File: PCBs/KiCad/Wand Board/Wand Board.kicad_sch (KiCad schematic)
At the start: 24 parts, among them J1 BRL LEDS, J10 ENC BTN, J11 ENCODER, J12 POW_IN, J13 BRL SENSE, J14 BAR, J15 DISP, J16 USB DATA, J2 BODY LEDS, J3 TIP LED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

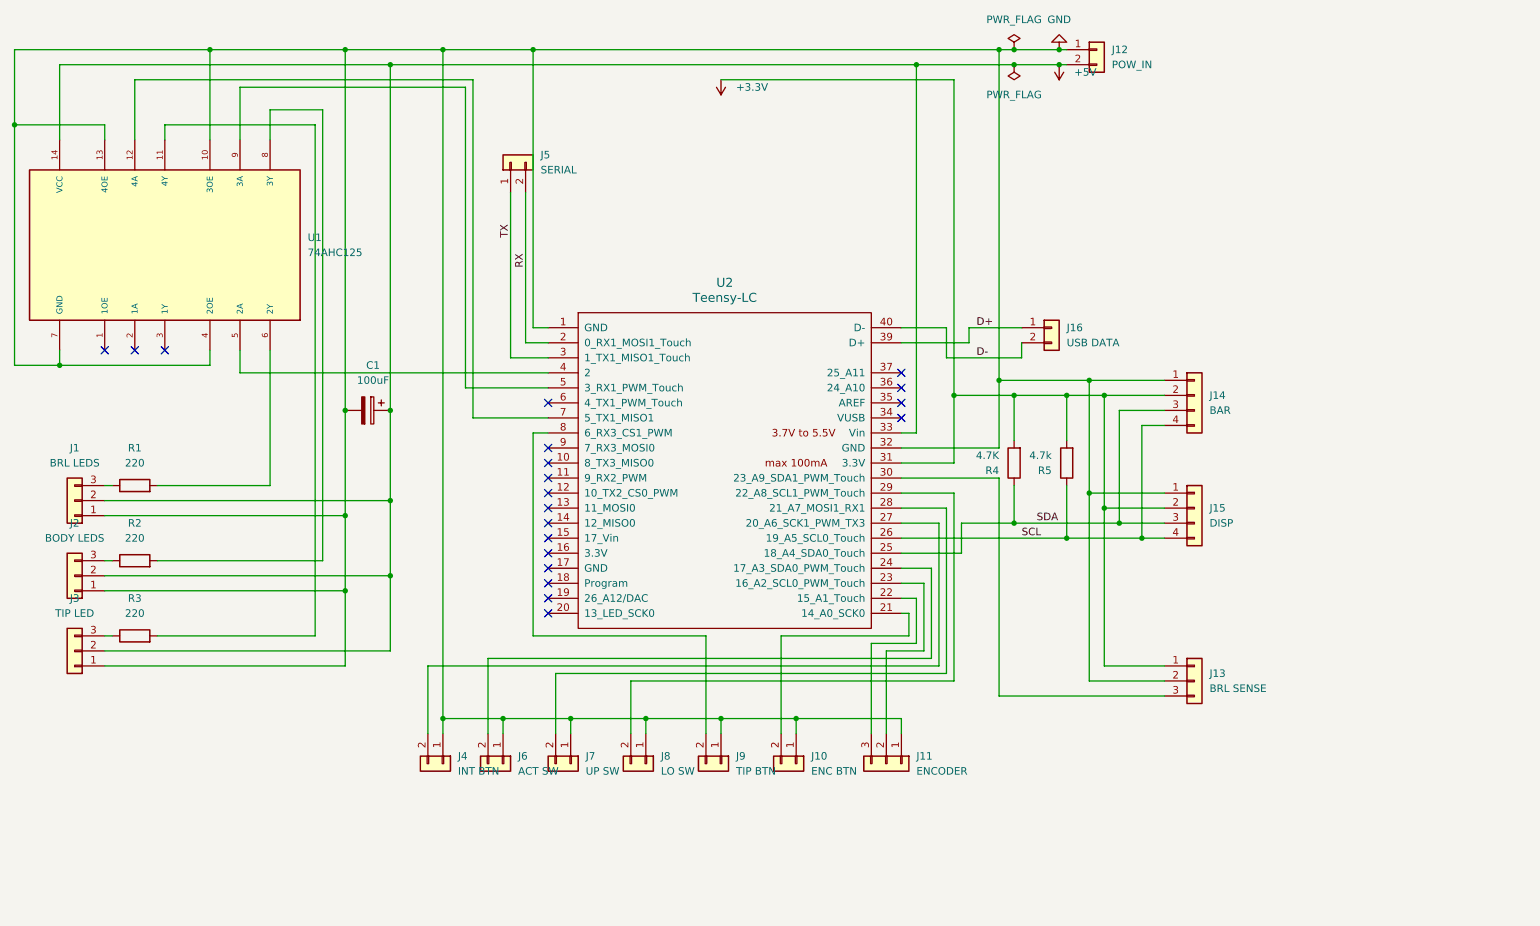
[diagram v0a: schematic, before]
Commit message: Updated Wand Board PCB: Migrate to Teensy 4.0, Change Encoder Pin Order
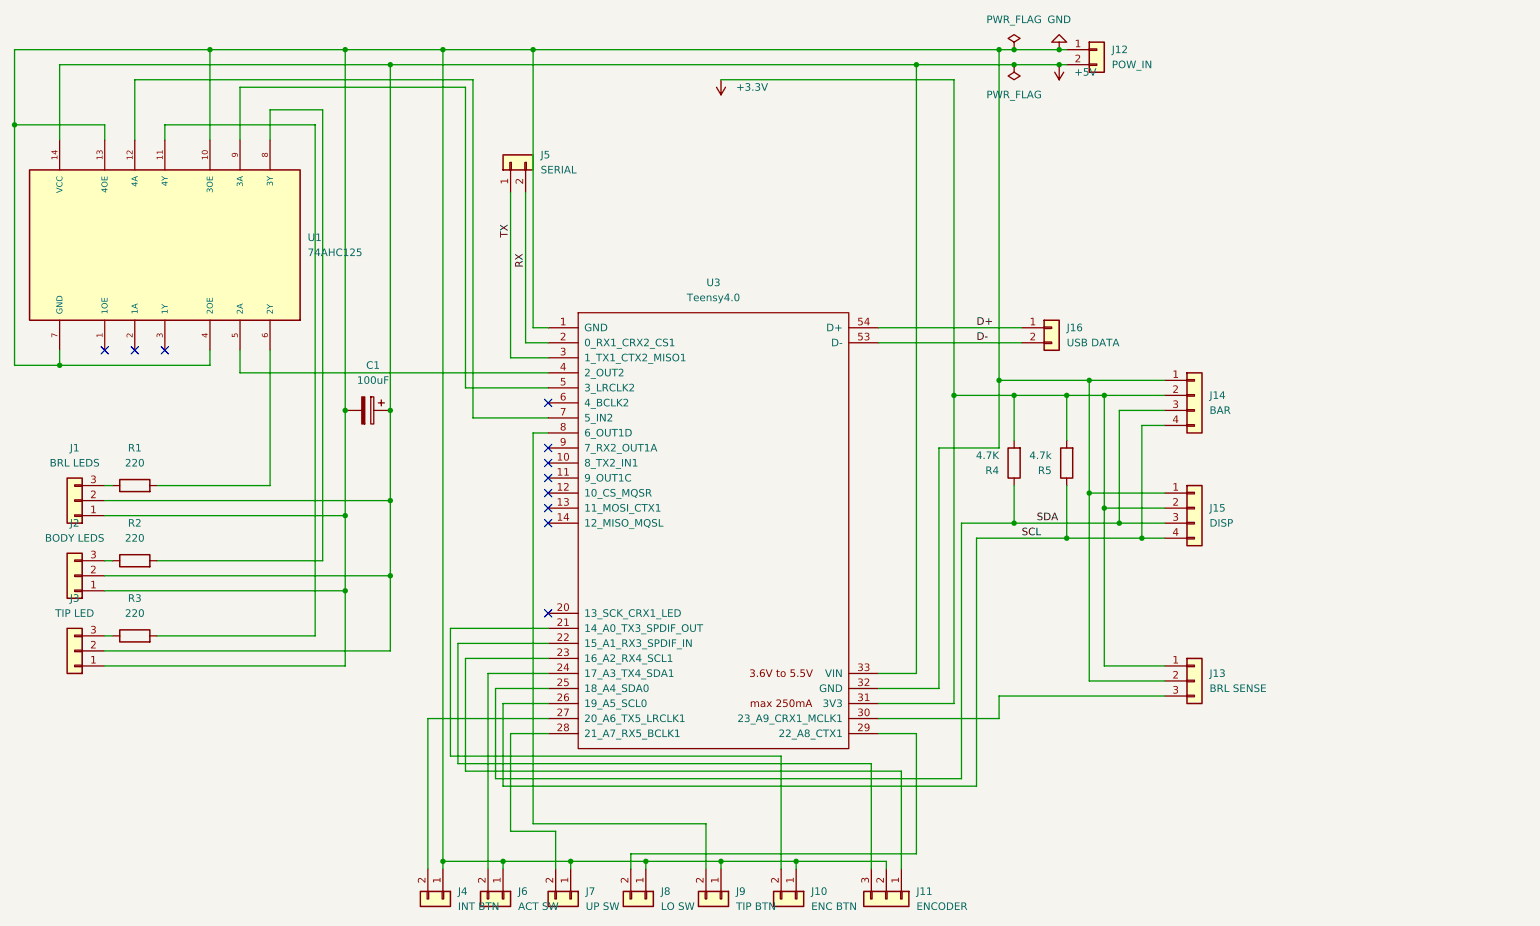
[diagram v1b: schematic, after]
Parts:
- removed U2: Teensy-LC, Teensy:Teensy_LC, symbol teensy:Teensy-LC
- added U3: Teensy4.0, Teensy:Teensy40-DHolesOnly, symbol teensy:Teensy4.0
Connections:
- net +3.3V: now also U3.31 (3V3)
- net +5V: now also U3.33 (VIN)
- net D+: now also U3.54 (D+)
- net D-: now also U3.53 (D-)
- net GND: now also J11.2 (Pin_2), U3.1 (GND), U3.32 (GND); no longer J11.1 (Pin_1)
- net RX: now also U3.2 (0_RX1_CRX2_CS1)
- net SCL: now also U3.26 (19_A5_SCL0)
- net SDA: now also U3.25 (18_A4_SDA0)
- net TX: now also U3.3 (1_TX1_CTX2_MISO1)
- net at J10.2 (Pin_2): now also U3.21 (14_A0_TX3_SPDIF_OUT)
- net at J11.3 (Pin_3): now also U3.22 (15_A1_RX3_SPDIF_IN)
- net at J6.2 (Pin_2): now also U3.24 (17_A3_TX4_SDA1)
- net at J4.2 (Pin_2): now also U3.27 (20_A6_TX5_LRCLK1)
- net at J7.2 (Pin_2): now also U3.28 (21_A7_RX5_BCLK1)
- net at J8.2 (Pin_2): now also U3.29 (22_A8_CTX1)
- net at J13.3 (Pin_3): now also U3.30 (23_A9_CRX1_MCLK1)
- net at U1.5 (2A): now also U3.4 (2_OUT2)
- net at U1.9 (3A): now also U3.5 (3_LRCLK2)
- net at U1.12 (4A): now also U3.7 (5_IN2)
- net at J9.2 (Pin_2): now also U3.8 (6_OUT1D)
- new net: J11.1 (Pin_1), U3.23 (16_A2_RX4_SCL1)
- no-connect marks 20 -> 11
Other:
- moved on the sheet: J10, J11, J4, J6, J7, J8, J9

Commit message: Added motor output for wand rumble
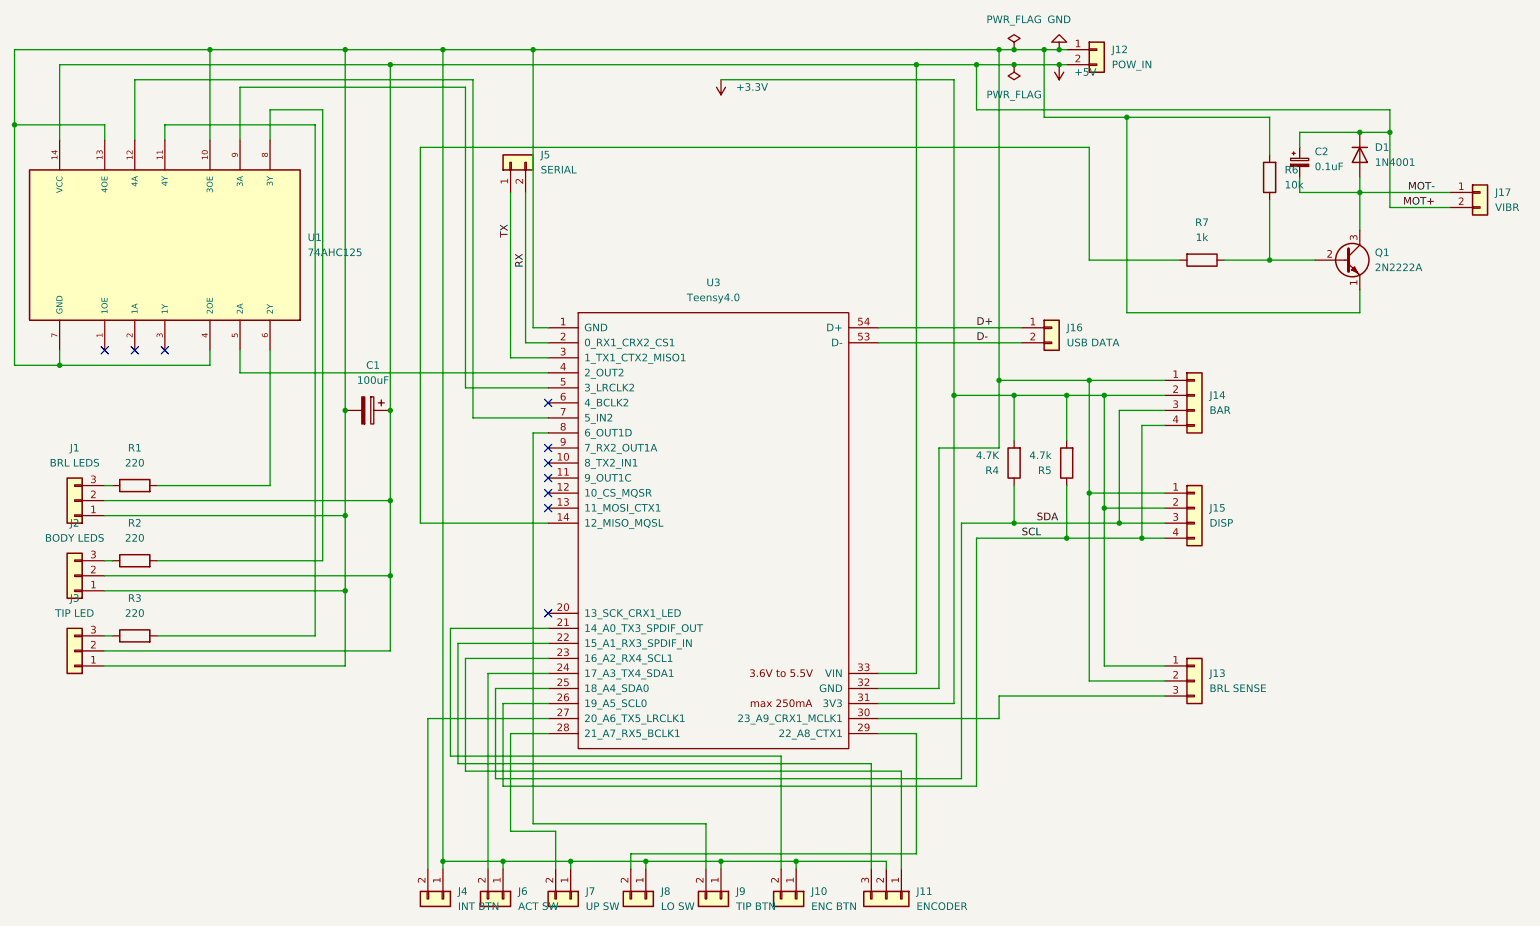
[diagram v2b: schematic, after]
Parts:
- added C2: 0.1uF, Capacitor_THT:CP_Radial_D4.0mm_P2.00mm, symbol Device:C_Polarized_Small
- added D1: 1N4001, Diode_THT:D_DO-41_SOD81_P10.16mm_Horizontal, symbol Diode:1N4001
- added J17: VIBR, Connector_JST:JST_XH_B2B-XH-A_1x02_P2.50mm_Vertical, symbol Connector_Generic:Conn_01x02
- added Q1: 2N2222A, Package_TO_SOT_THT:TO-92_Inline, symbol Transistor_BJT:PN2222A
- added R6: 10k, Resistor_THT:R_Axial_DIN0207_L6.3mm_D2.5mm_P7.62mm_Horizontal, symbol Device:R
- added R7: 1k, Resistor_THT:R_Axial_DIN0207_L6.3mm_D2.5mm_P7.62mm_Horizontal, symbol Device:R
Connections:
- net +5V: now also C2.1, D1.1 (K), J17.2 (Pin_2)
- net GND: now also Q1.1 (E), R6.2
- net at U3.14 (12_MISO_MQSL): now also R7.2
- new net: Q1.2 (B), R6.1, R7.1
- new net MOT-: C2.2, D1.2 (A), J17.1 (Pin_1), Q1.3 (C)
- no-connect marks 11 -> 10

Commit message: Added additional i2c output to wand board for optional driver
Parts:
- added J18: i2c, Connector_JST:JST_XH_B4B-XH-A_1x04_P2.50mm_Vertical, symbol Connector_Generic:Conn_01x04
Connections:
- net +3.3V: now also J18.2 (Pin_2)
- net GND: now also J18.1 (Pin_1)
- net SCL: now also J18.4 (Pin_4)
- net SDA: now also J18.3 (Pin_3)
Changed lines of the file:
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@@
   (junction (at 250.19 31.75) (diameter 0) (color 0 0 0 0)
   )
+  (junction (at 201.93 109.22) (diameter 0) (color 0 0 0 0)
+  )
   (junction (at 199.39 92.71) (diameter 0) (color 0 0 0 0)
   )
   (junction (at 186.69 20.32) (diameter 0) (color 0 0 0 0)
+  )
+  (junction (at 199.39 106.68) (diameter 0) (color 0 0 0 0)
   )
   (junction (at 100.33 154.94) (diameter 0) (color 0 0 0 0)
@@
     (stroke (width 0) (type default))
   )
-  (wire (pts (xy 201.93 95.25) (xy 201.93 121.92))
+  (wire (pts (xy 199.39 106.68) (xy 212.09 106.68))
+    (stroke (width 0) (type default))
+  )
+  (wire (pts (xy 201.93 95.25) (xy 201.93 109.22))
     (stroke (width 0) (type default))
   )
@@
     (stroke (width 0) (type default))
   )
+  (wire (pts (xy 208.28 114.3) (xy 208.28 100.33))
+    (stroke (width 0) (type default))
+  )
   (wire (pts (xy 101.6 41.91) (xy 101.6 69.85))
     (stroke (width 0) (type default))
@@
     (stroke (width 0) (type default))
   )
+  (wire (pts (xy 212.09 114.3) (xy 208.28 114.3))
+    (stroke (width 0) (type default))
+  )
   (wire (pts (xy 163.83 133.35) (xy 170.18 133.35))
     (stroke (width 0) (type default))
@@
     (stroke (width 0) (type default))
   )
-  (wire (pts (xy 199.39 92.71) (xy 199.39 124.46))
+  (wire (pts (xy 199.39 92.71) (xy 199.39 106.68))
     (stroke (width 0) (type default))
   )
@@
     (stroke (width 0) (type default))
   )
+  (wire (pts (xy 212.09 111.76) (xy 204.47 111.76))
+    (stroke (width 0) (type default))
+  )
   (wire (pts (xy 91.44 115.57) (xy 107.95 115.57))
     (stroke (width 0) (type default))
@@
     (stroke (width 0) (type default))
   )
+  (wire (pts (xy 201.93 109.22) (xy 201.93 121.92))
+    (stroke (width 0) (type default))
+  )
   (wire (pts (xy 199.39 73.66) (xy 212.09 73.66))
     (stroke (width 0) (type default))
@@
     (stroke (width 0) (type default))
   )
+  (wire (pts (xy 201.93 109.22) (xy 212.09 109.22))
+    (stroke (width 0) (type default))
+  )
   (wire (pts (xy 199.39 53.34) (xy 214.63 53.34))
     (stroke (width 0) (type default))
@@
     (stroke (width 0) (type default))
   )
+  (wire (pts (xy 199.39 106.68) (xy 199.39 124.46))
+    (stroke (width 0) (type default))
+  )
   (wire (pts (xy 163.83 64.77) (xy 187.96 64.77))
     (stroke (width 0) (type default))
@@
   )
   (wire (pts (xy 101.6 133.35) (xy 101.6 149.86))
+    (stroke (width 0) (type default))
+  )
+  (wire (pts (xy 204.47 111.76) (xy 204.47 97.79))
     (stroke (width 0) (type default))
   )
@@
         )
       )
+    )
+  )
+  (symbol (lib_id "Connector_Generic:Conn_01x04") (at 217.17 109.22 0) (unit 1)
+    (in_bom yes) (on_board yes) (dnp no) (fields_autoplaced)
+    (property "Reference" "J18" (at 219.71 109.22 0)
+      (effects (font (size 1.27 1.27)) (justify left))
+    )
+    (property "Value" "i2c" (at 219.71 111.76 0)
+      (effects (font (size 1.27 1.27)) (justify left))
+    )
+    (property "Footprint" "Connector_JST:JST_XH_B4B-XH-A_1x04_P2.50mm_Vertical" (at 217.17 109.22 0)
+      (effects (font (size 1.27 1.27)) hide)
+    )
+    (property "Datasheet" "~" (at 217.17 109.22 0)
+      (effects (font (size 1.27 1.27)) hide)
+    )
+    (pin "1")
+    (pin "2")
+    (pin "3")
+    (pin "4")
+    (instances
+      (project "Wand Board"
+        (path "/1c8798cf-59eb-4db0-a440-e8dd7a851253"
+          (reference "J18") (unit 1)
+        )
+      )
